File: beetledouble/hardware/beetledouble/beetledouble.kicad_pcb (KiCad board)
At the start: 4 copper layers, 32 x 60 mm, 63 parts, among them J1 XT30PW-M, J2 rxin, J4 motor_out, J5 motor_out, J6 prog connector, Q1 SE3082G, Q2 SE3082G, Q3 SE3082G, Q4 SE3082G, U1 78L12G-AB3-R, U2 DD4012SB, U3 ATtiny1614-SS, U4 NCP81155MN, U5 NCP81155MN, U6 NCP81155MN, U7 NCP81155MN

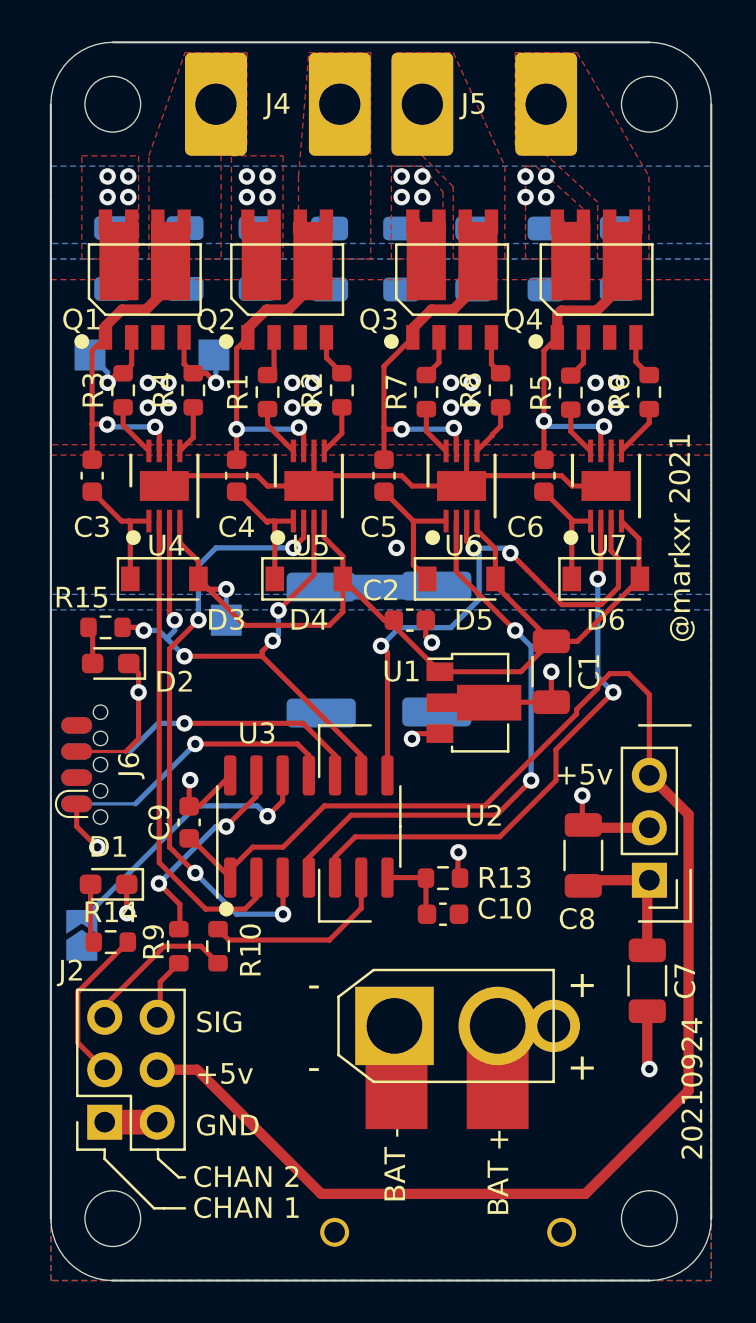
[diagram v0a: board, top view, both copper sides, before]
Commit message: Beetledouble: further board design tweaks
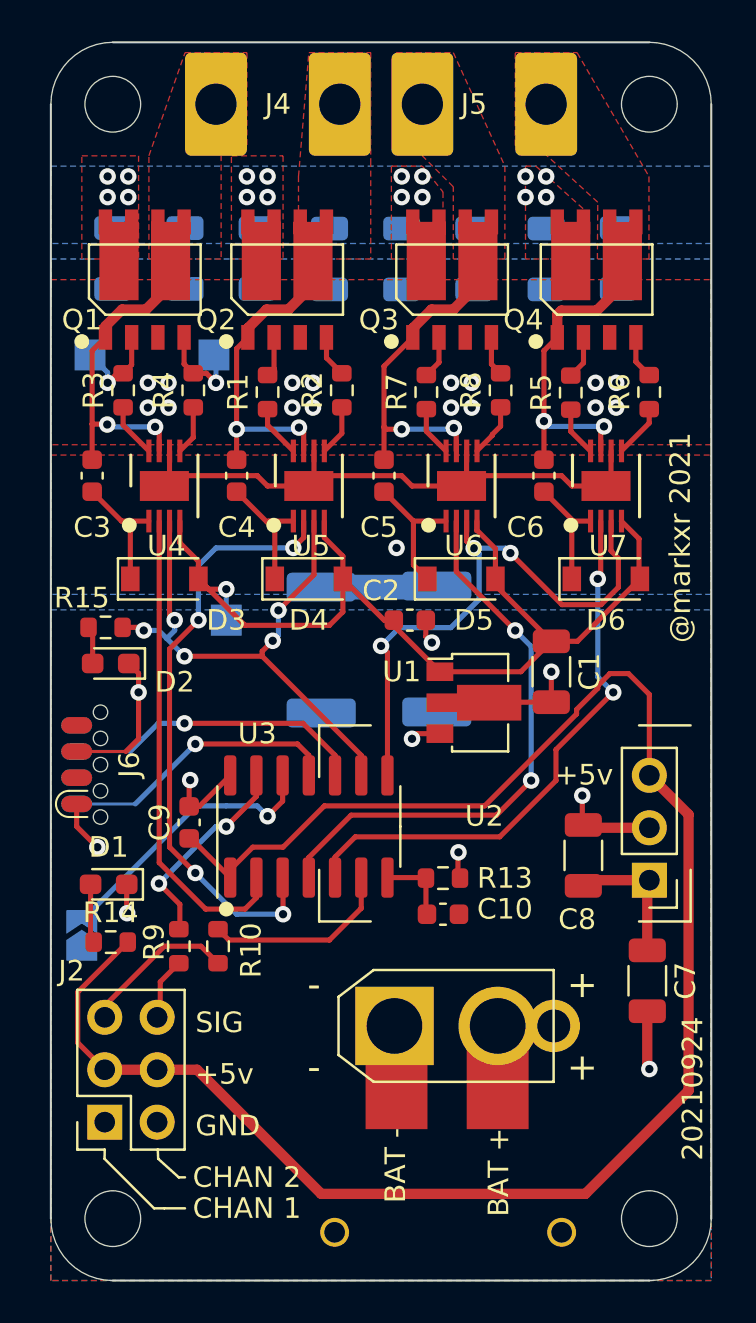
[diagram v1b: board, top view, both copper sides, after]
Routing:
- net GND: track 59.9 -> 57.3 mm
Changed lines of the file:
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@@
   (gr_circle (center 114 85.5) (end 114.3 85.5) (layer "F.SilkS") (width 0.12) (fill solid))
   (gr_circle (center 129 85.5) (end 129.3 85.5) (layer "F.SilkS") (width 0.12) (fill solid))
-  (gr_circle (center 109.5 95) (end 109.8 95) (layer "F.SilkS") (width 0.12) (fill solid))
-  (gr_circle (center 124 95) (end 124.3 95) (layer "F.SilkS") (width 0.12) (fill solid))
+  (gr_circle (center 109.3 94.4) (end 109.6 94.4) (layer "F.SilkS") (width 0.12) (fill solid))
+  (gr_circle (center 123.8 94.4) (end 124.1 94.4) (layer "F.SilkS") (width 0.12) (fill solid))
   (gr_line (start 110.7 125.1) (end 111.7 126) (layer "F.SilkS") (width 0.12))
   (gr_line (start 108.11 124.655) (end 108.1 125.1) (layer "F.SilkS") (width 0.12))
-  (gr_circle (center 116.5 95) (end 116.8 95) (layer "F.SilkS") (width 0.12) (fill solid))
+  (gr_circle (center 116.3 94.4) (end 116.6 94.4) (layer "F.SilkS") (width 0.12) (fill solid))
   (gr_circle (center 122 85.5) (end 122.3 85.5) (layer "F.SilkS") (width 0.12) (fill solid))
-  (gr_circle (center 130.7 95) (end 131 95) (layer "F.SilkS") (width 0.12) (fill solid))
+  (gr_circle (center 130.7 94.4) (end 131 94.4) (layer "F.SilkS") (width 0.12) (fill solid))
   (gr_circle (center 114 113) (end 114.3 113) (layer "F.SilkS") (width 0.12) (fill solid))
   (gr_circle (center 107 85.5) (end 107.3 85.5) (layer "F.SilkS") (width 0.12) (fill solid))
@@
   (via (at 114 97.5) (size 0.8) (drill 0.4) (layers "F.Cu" "B.Cu") (net 1))
   (segment (start 114 99) (end 114 97.5) (width 0.25) (layer "B.Cu") (net 1))
-  (segment (start 108.11 123.325) (end 110.65 123.325) (width 1.2) (layer "F.Cu") (net 2))
   (segment (start 122.5 92) (end 118.5 92) (width 0.25) (layer "F.Cu") (net 2))
   (segment (start 107.25 105.365) (end 109.135 105.365) (width 0.15) (layer "F.Cu") (net 2))
@@
   (segment (start 112.29 109.575) (end 114.19 111.475) (width 0.25) (layer "F.Cu") (net 4))
   (segment (start 130.97452 103.332621) (end 130.97452 103.545046) (width 0.25) (layer "F.Cu") (net 4))
+  (segment (start 110.65 120.785) (end 108.11 120.785) (width 0.5) (layer "F.Cu") (net 4))
   (segment (start 110.65 120.785) (end 112.585 120.785) (width 0.5) (layer "F.Cu") (net 4))
   (segment (start 106.8 119.475) (end 108.11 120.785) (width 0.25) (layer "F.Cu") (net 4))
@@
   (segment (start 115.281854 110) (end 114.19 111.091854) (width 0.25) (layer "F.Cu") (net 4))
   (segment (start 136.4 121.8) (end 136.4 108.42) (width 0.5) (layer "F.Cu") (net 4))
-  (segment (start 108.11 120.785) (end 110.65 120.785) (width 1.2) (layer "In2.Cu") (net 4))
   (segment (start 120.54 112.96) (end 120.54 111.475) (width 0.25) (layer "F.Cu") (net 5))
   (segment (start 119 114.5) (end 120.54 112.96) (width 0.25) (layer "F.Cu") (net 5))

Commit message: Minor pcb tweaks for better reliability solderability etc
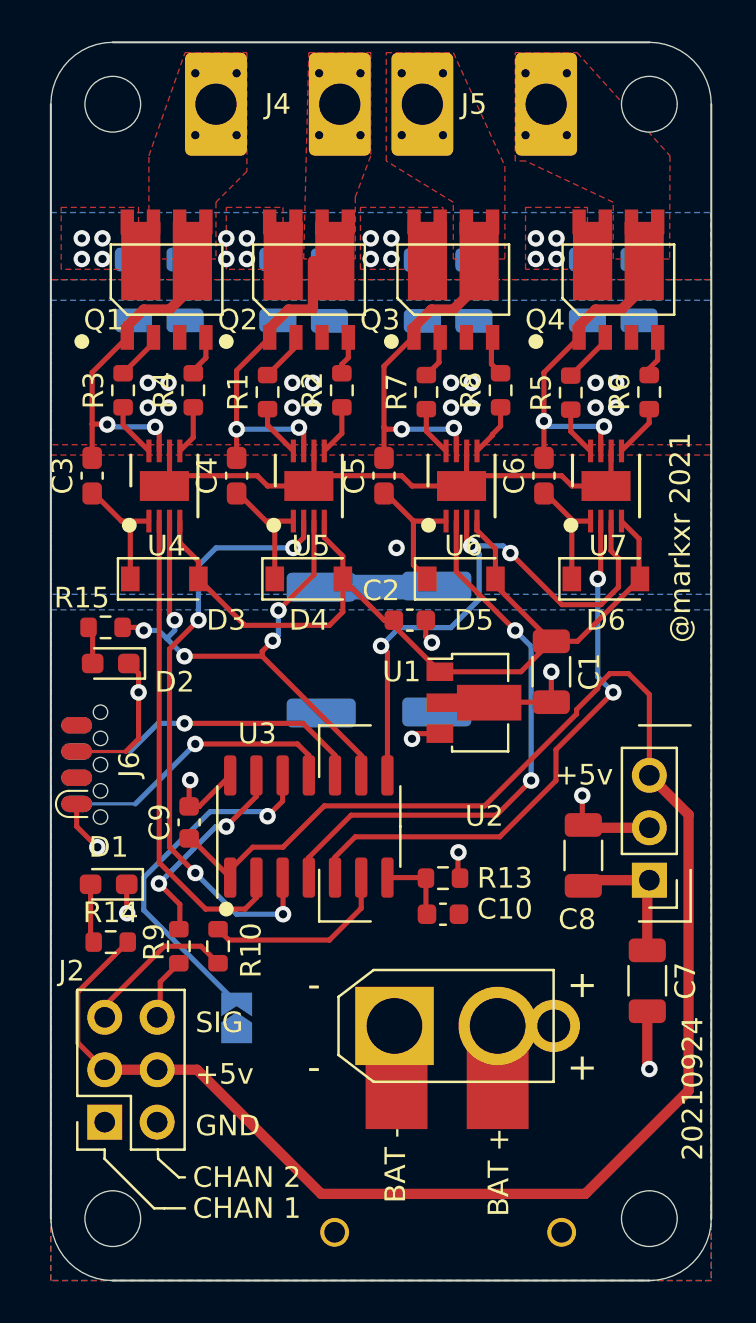
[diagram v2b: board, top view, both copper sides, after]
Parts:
- removed TP1, TP2, TP3: TestPoint, TestPoint:TestPoint_Pad_1.5x1.5mm
- C3, C4, C5, C6: value 2.2uF 50V -> 4.7uF 50V; footprint Capacitor_SMD:C_0603_1608Metric -> Capacitor_SMD:C_0603_1608Metric_Pad1.08x0.95mm_HandSolder
- moved JP1 8.50 mm to (114.5, 118.3)
- moved C15 2.50 mm to (131.5, 83.0)
- moved C11 1.82 mm to (109.5, 83.0)
- moved C12 1.82 mm to (116.5, 83.0)
- moved C14 1.82 mm to (123.5, 83.0)
- moved C18 1.82 mm to (134.0, 83.0)
- moved C13 1.53 mm to (112.0, 83.0)
- moved C16 1.53 mm to (126.0, 83.0)
- moved C17 1.53 mm to (119.0, 83.0)
- moved Q1 1.06 mm to (111.1, 82.5)
- moved Q4 1.06 mm to (133.0, 82.5)
- moved Q2 1.06 mm to (118.0, 82.5)
- moved Q3 0.06 mm to (125.0, 82.5)
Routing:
- net CONFIG1: track 13.8 -> 17.6 mm
- net +12V: track 48.0 -> 44.9 mm, vias 1 -> 0
- net /driver1/GATEL1: track 4.60 -> 1.99 mm, vias 1 -> 0
- net /driver1/GATEH1: track 4.55 -> 2.35 mm, vias 1 -> 0
- net /driver1/MOTORS1: track 16.2 -> 15.7 mm

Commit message: Hardware misc updates
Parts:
- moved J4 0.50 mm to (114.0, 74.0)
- moved J5 0.50 mm to (124.0, 74.0)
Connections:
- J6 pad 1: VBAT -> +5V
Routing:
- net +5V: track 88.6 -> 97.9 mm
- net VBAT: track 10.6 -> 8.11 mm, vias 18 -> 17
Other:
- board text removed: "20210924"

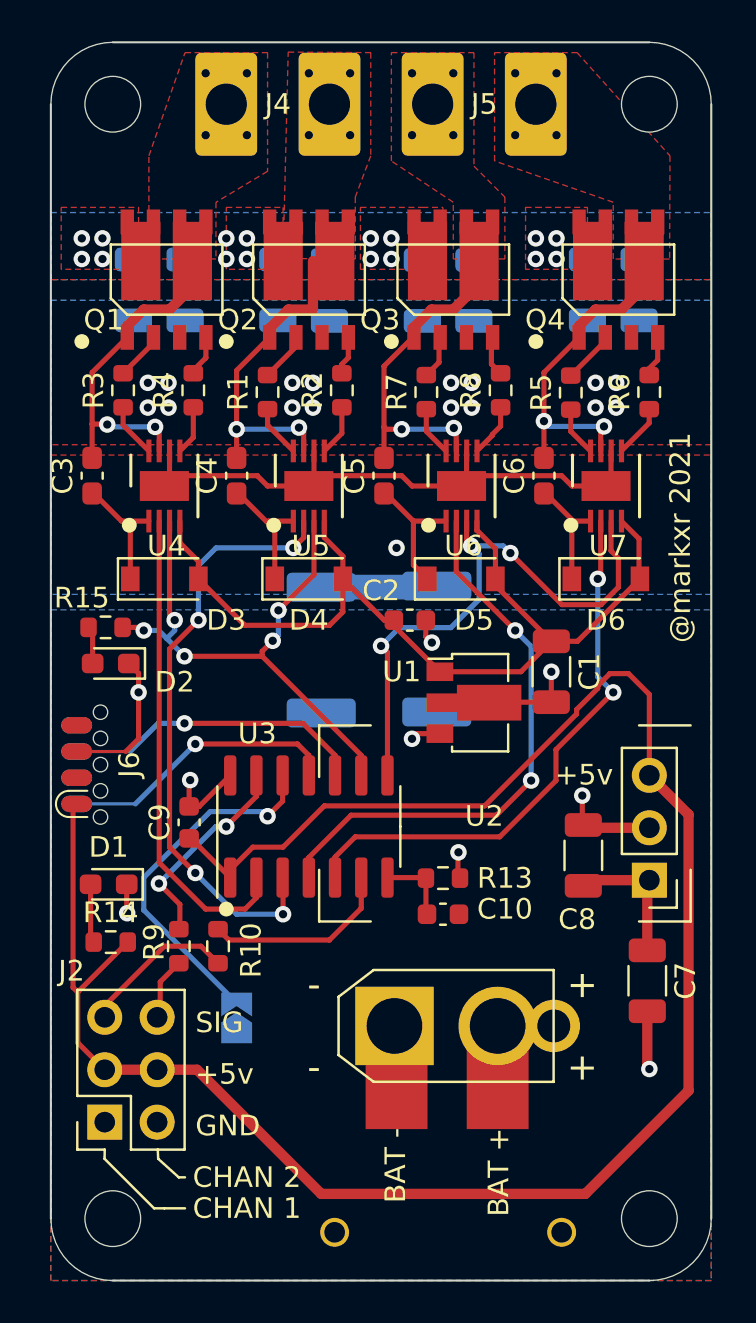
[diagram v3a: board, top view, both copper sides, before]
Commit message: Pin updates to get ADC pins and VSENSE and ISENSE etc
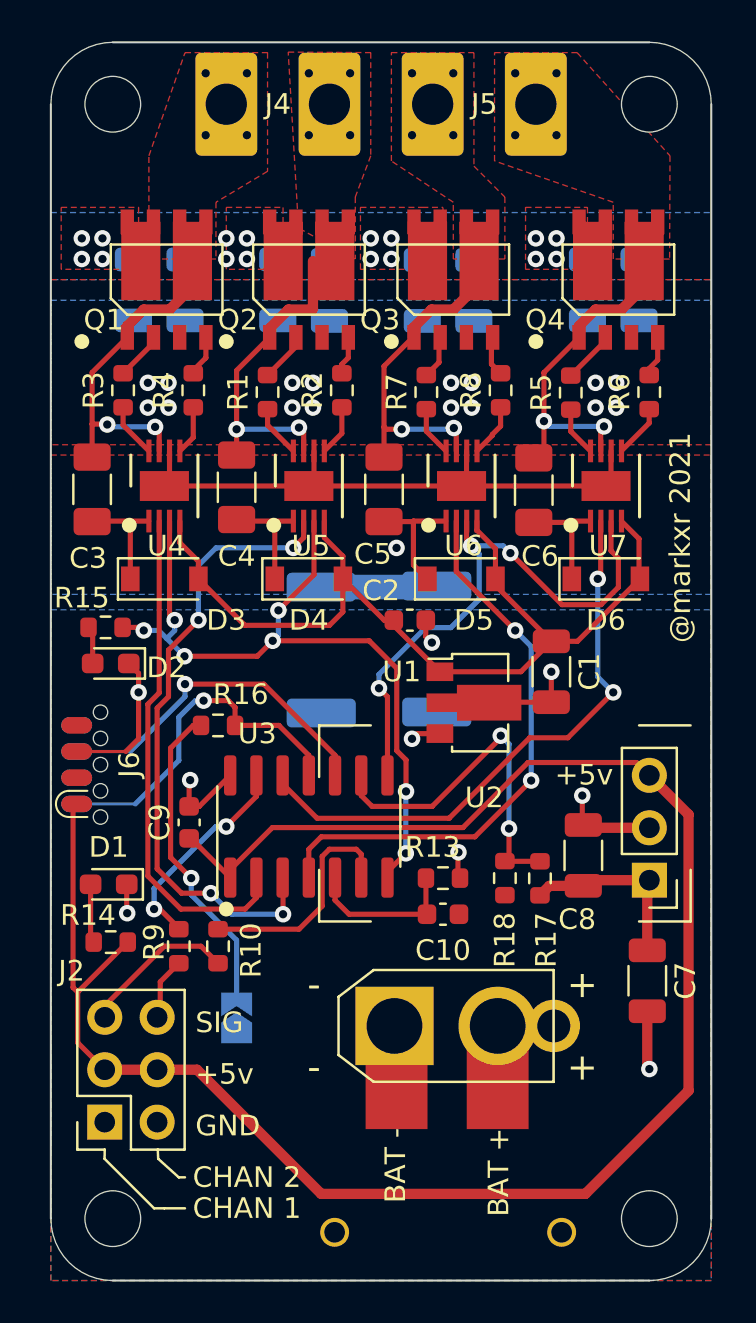
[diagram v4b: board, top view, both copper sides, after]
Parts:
- added R16: 22k, Resistor_SMD:R_0603_1608Metric, F.Cu at (113.6, 104.1)
- added R17: 22k, Resistor_SMD:R_0603_1608Metric, F.Cu at (129.2, 111.5)
- added R18: 1k, Resistor_SMD:R_0603_1608Metric, F.Cu at (127.5, 111.5)
- C3, C4, C5, C6: footprint Capacitor_SMD:C_0603_1608Metric_Pad1.08x0.95mm_HandSolder -> Capacitor_SMD:C_1206_3216Metric_Pad1.33x1.80mm_HandSolder
- moved C6 0.86 mm to (128.9, 92.7)
- moved C3 0.66 mm to (107.5, 92.7)
- moved C5 0.66 mm to (121.6, 92.7)
- moved C4 0.56 mm to (114.5, 92.6)
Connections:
- JP1 pad 2: CONFIG1 -> /CONFIG1
- U3 pad 12: CONFIG1 -> MOTORR_2
- U3 pad 5: MOTORR_2 -> /ISENSE
- U3 pad 7: /ISENSE -> MOTOR_ENABLE_1
- U3 pad 9: MOTOR_ENABLE_1 -> /VSENSE
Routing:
- net CONFIG1: track 17.6 -> 0.00 mm, vias 1 -> 0
- net /VSENSE: track 0.00 -> 17.5 mm, vias 0 -> 2
- net /CONFIG1: track 0.00 -> 15.6 mm, vias 0 -> 1
- net MOTOR_ENABLE_1: track 28.6 -> 38.0 mm, vias 5 -> 7
- net +5V: track 97.9 -> 91.8 mm
- net /ISENSE: track 3.59 -> 7.60 mm
- net TXDEBUG: track 13.2 -> 16.6 mm
- net VBAT: track 8.11 -> 10.4 mm
- net UPDI: track 14.2 -> 16.1 mm
- net PWMIN_1: track 9.28 -> 11.2 mm
- net MOTORR_1: track 29.3 -> 30.8 mm
- net GND: track 57.3 -> 56.1 mm
- net MOTORF_1: track 23.4 -> 24.6 mm
- net MOTORR_2: track 27.3 -> 28.3 mm
- net MOTOR_ENABLE_2: track 28.2 -> 27.5 mm
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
